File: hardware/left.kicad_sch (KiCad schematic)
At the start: 0 parts

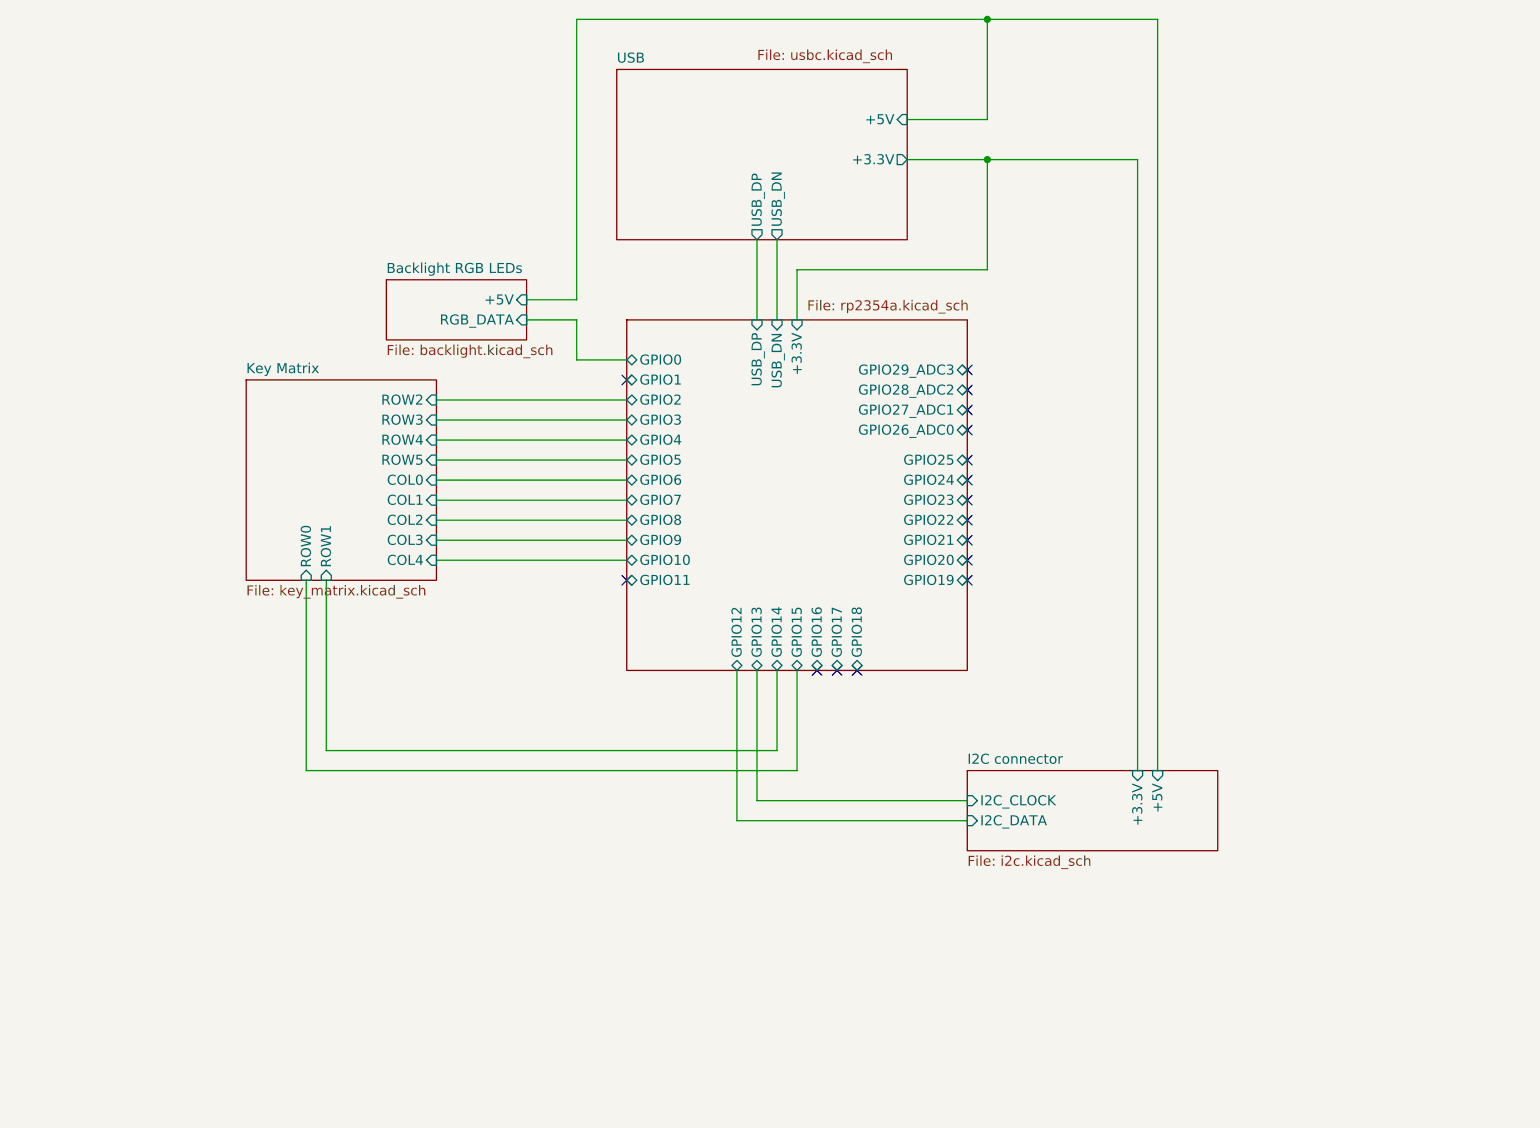
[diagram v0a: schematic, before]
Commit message: encoder to schematic
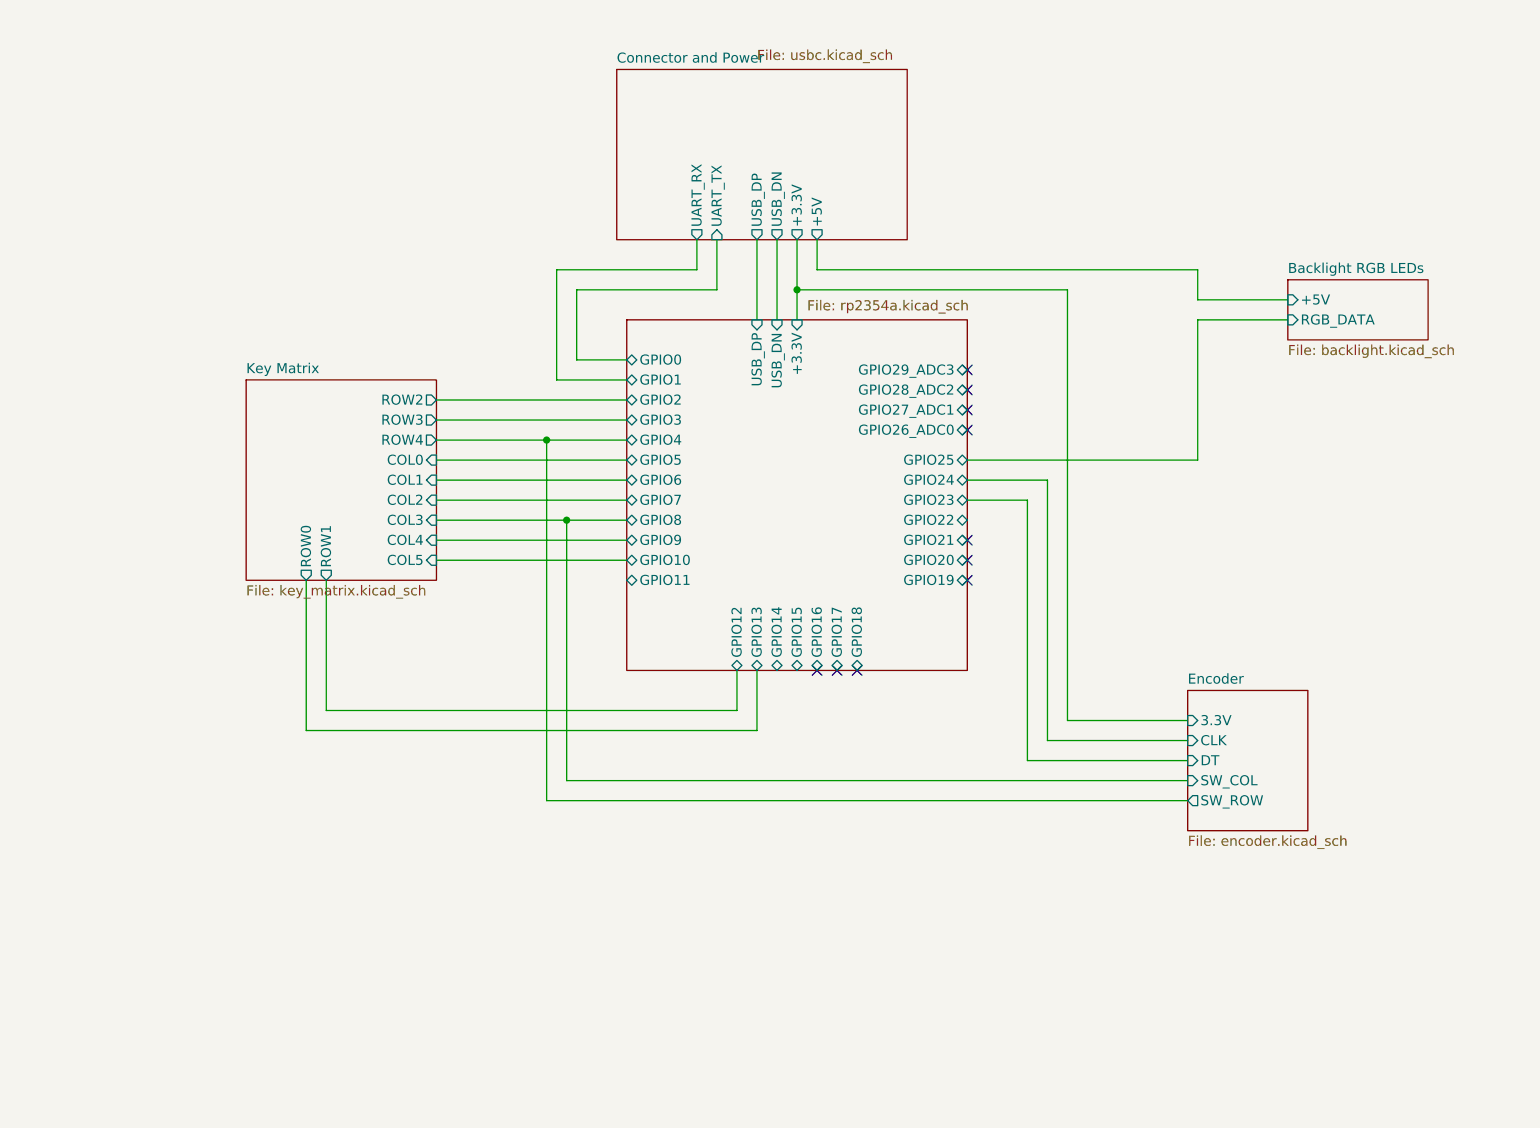
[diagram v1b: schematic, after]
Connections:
- no-connect marks 16 -> 10
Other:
- sheet USB renamed Connector and Power
- removed sheet I2C connector
- added sheet Encoder (encoder.kicad_sch)
- sheet Connector and Power ports: added UART_RX, UART_TX; removed none
- sheet Key Matrix ports: added COL5; removed ROW5

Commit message: electronics
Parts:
- added PCB shape left1: (no value), rp_voyager:PCB left, symbol rp_voyager:PCB_left
- added Realestateleft1: (no value), rp_voyager:Realestate left, symbol rp_voyager:realestate_left
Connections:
- no-connect marks 10 -> 18
